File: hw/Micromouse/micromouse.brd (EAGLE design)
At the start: 60 x 112 mm, 44 parts, among them IC1 DSPIC33FJ64MC804-PT, IC2 DRV8833PWR, J1 GP2Y0A51SK0F, J2 GP2Y0A51SK0F, J3 GP2Y0A41SK0F, SW1 B3F-1000

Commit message: Updated PCB
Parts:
- added C15, C16, C17: (no value), micromouse:0805_POL
- moved C12 29.2 mm to (-5.00, -38.2), turned to 270 degrees
- moved SW1 27.6 mm to (-0.04, -36.9)
- moved R4 26.9 mm to (-7.20, -36.0)
- moved R5 21.4 mm to (-5.00, -33.8), turned to 90 degrees
- moved R3 11.8 mm to (-19.6, 40.9), turned to 90 degrees
- moved SW_RST 10.3 mm to (-25.4, 38.6), turned to 0 degrees
- moved R2 10.0 mm to (-25.4, 44.7), turned to 331.7 degrees
- moved LED1 9.80 mm to (0.00, 51.2)
- moved D4 9.47 mm to (-24.4, 47.7), turned to 151.7 degrees
- moved D3 9.46 mm to (-23.4, 49.6), turned to 151.7 degrees
- moved D2 9.45 mm to (-22.4, 51.4), turned to 151.7 degrees
- moved D1 9.44 mm to (-21.5, 53.2), turned to 151.7 degrees
- moved R9 9.42 mm to (-21.0, 45.6), turned to 331.7 degrees
- moved R8 9.41 mm to (-20.0, 47.6), turned to 331.7 degrees
- moved R7 9.41 mm to (-19.0, 49.6), turned to 331.7 degrees
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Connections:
- net +5V: now also C15.1, C16.1, C17.1
- net GND: now also C15.2, C16.2, C17.2
- net S1_OUT: now also IC1.22; no longer IC1.20
- net S3_OUT: now also IC1.20; no longer IC1.22
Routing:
- net +3V3: track 267.4 -> 279.6 mm, vias 5 -> 4
- net SW1: track 54.9 -> 66.8 mm, vias 4 -> 2
- net +5V: track 118.8 -> 125.7 mm
- net GND: track 52.7 -> 58.3 mm, vias 19 -> 20
- net S1_OUT: track 21.6 -> 27.3 mm
- net S2_OUT: track 19.1 -> 22.3 mm
- net N$7: track 10.8 -> 13.6 mm
- net LED4: track 15.7 -> 17.6 mm
- net N$6: track 7.98 -> 9.81 mm
- net LED3: track 16.3 -> 18.0 mm
- net S3_OUT: track 10.2 -> 8.64 mm
- net +9V: track 88.2 -> 87.0 mm
- net LED2: track 17.0 -> 18.0 mm
- net MCLR: track 31.7 -> 31.0 mm
- net M2-: track 16.3 -> 16.9 mm
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- added copper zone on layer 1, net GND
- added copper zone on layer 16, net GND
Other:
- board size 60 x 112 mm -> 60 x 97 mm

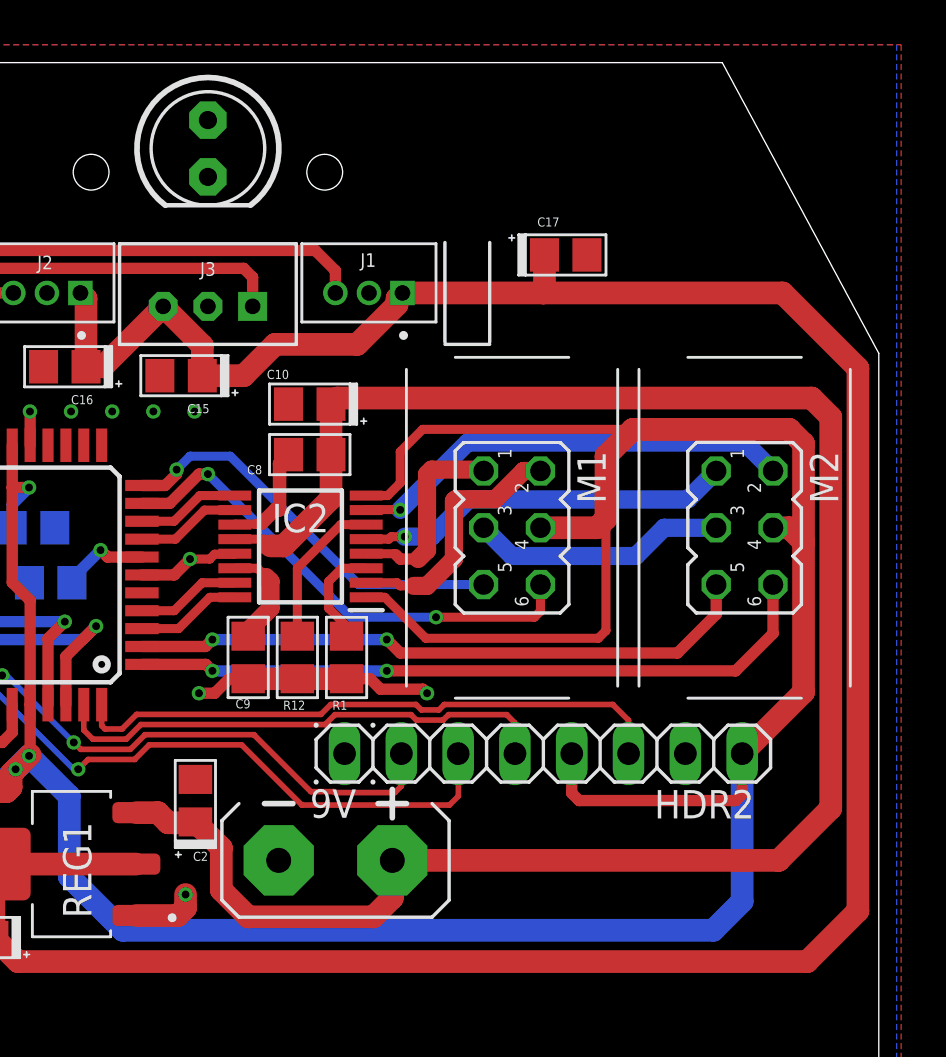
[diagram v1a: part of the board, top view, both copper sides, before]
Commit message: Added hole for routing wires of battery connector
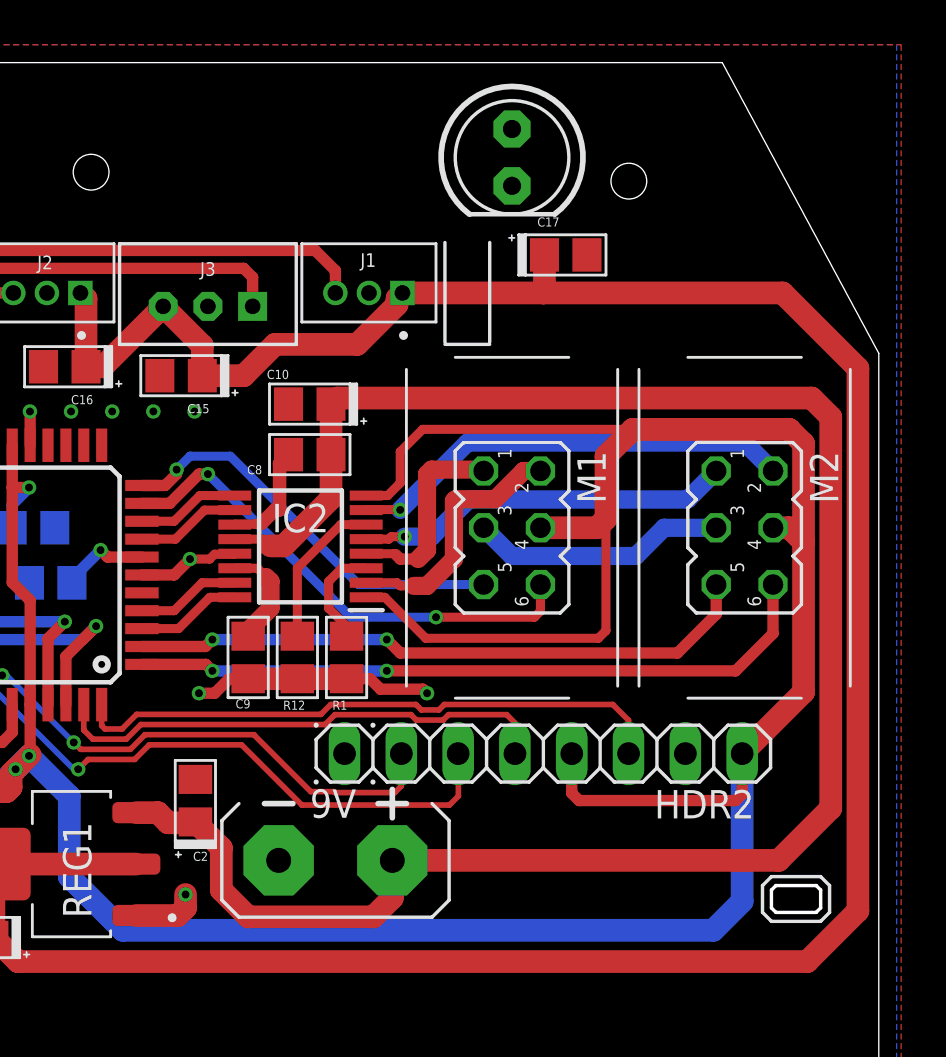
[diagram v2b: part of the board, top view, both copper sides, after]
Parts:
- moved LED1 13.6 mm to (13.6, 50.8)
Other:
- outline, holes or cut-outs redrawn
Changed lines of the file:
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@@
 <drawing>
 <settings>
-<setting alwaysvectorfont="no"/>
+<setting alwaysvectorfont="yes"/>
 <setting verticaltext="up"/>
 </settings>
@@
 </layers>
 <board>
-<fusionsync huburn="a.YnVzaW5lc3M6bXl0dW05MzU" projecturn="a.YnVzaW5lc3M6bXl0dW05MzUjMjAyMTAxMTgzNzI4NzA0MjY" f3durn="urn:adsk.wipprod:dm.lineage:L23jFv8gR_u2aycr5DJv9Q" pcbguid="" lastpulledtime="2021-02-11T09:58:18Z" lastsyncedchangeguid="" latestrevisionid="4fbf5507-91a6-4be1-affa-b37500ad01a3" lastsyncedrevisionid="4fbf5507-91a6-4be1-affa-b37500ad01a3" lastboardhashguid="931b2172-0a8d-4494-72eb-2a34aca0cbeb" lastpushedtime="2021-02-11T20:43:38Z" linktopcb3d="true"/>
+<fusionsync huburn="a.YnVzaW5lc3M6bXl0dW05MzU" projecturn="a.YnVzaW5lc3M6bXl0dW05MzUjMjAyMTAxMTgzNzI4NzA0MjY" f3durn="urn:adsk.wipprod:dm.lineage:L23jFv8gR_u2aycr5DJv9Q" pcbguid="" lastpulledtime="2021-02-11T09:58:18Z" lastsyncedchangeguid="" latestrevisionid="bb3ab1a6-1e4b-46e2-9ee9-392ab2f42304" lastsyncedrevisionid="bb3ab1a6-1e4b-46e2-9ee9-392ab2f42304" lastboardhashguid="8f49f6ad-d1e3-cec0-48bd-d1e4115f87a2" lastpushedtime="2021-02-16T11:45:34Z" linktopcb3d="true"/>
 <plain>
 <wire x1="10.598" y1="46.956" x2="10.598" y2="42.498" width="0.1524" layer="21"/>
@@
 <wire x1="12.6" y1="42.4" x2="10.6" y2="42.4" width="0.1524" layer="21"/>
 <wire x1="12.602" y1="46.956" x2="12.602" y2="42.498" width="0.1524" layer="21"/>
-<circle x="5.223" y="50.1" radius="0.8" width="0" layer="20"/>
+<circle x="18.823" y="49.7" radius="0.8" width="0" layer="20"/>
 <circle x="21" y="2" radius="0.8" width="0" layer="20"/>
 <circle x="21" y="-40" radius="0.8" width="0" layer="20"/>
@@
 <wire x1="23" y1="55" x2="-23" y2="55" width="0" layer="20"/>
 <wire x1="-23" y1="55" x2="-30" y2="42" width="0" layer="20"/>
+<wire x1="27.4" y1="18" x2="27.2" y2="18.2" width="0.1524" layer="20"/>
+<wire x1="27.2" y1="18.2" x2="25.4" y2="18.2" width="0.1524" layer="20"/>
+<wire x1="25.4" y1="18.2" x2="25.2" y2="18" width="0.1524" layer="20"/>
+<wire x1="25.2" y1="17.2" x2="25.4" y2="17" width="0.1524" layer="20"/>
+<wire x1="25.4" y1="17" x2="27.2" y2="17" width="0.1524" layer="20"/>
+<wire x1="27.2" y1="17" x2="27.4" y2="17.2" width="0.1524" layer="20"/>
+<wire x1="27.4" y1="18" x2="27.4" y2="17.2" width="0.1524" layer="20"/>
+<wire x1="25.2" y1="17.2" x2="25.2" y2="18" width="0.1524" layer="20"/>
+<wire x1="25.2" y1="18.6" x2="27.4" y2="18.6" width="0.1524" layer="21"/>
+<wire x1="27.4" y1="18.6" x2="27.8" y2="18.2" width="0.1524" layer="21"/>
+<wire x1="27.8" y1="18.2" x2="27.8" y2="17" width="0.1524" layer="21"/>
+<wire x1="27.8" y1="17" x2="27.4" y2="16.6" width="0.1524" layer="21"/>
+<wire x1="27.4" y1="16.6" x2="25.2" y2="16.6" width="0.1524" layer="21"/>
+<wire x1="25.2" y1="16.6" x2="24.8" y2="17" width="0.1524" layer="21"/>
+<wire x1="24.8" y1="17" x2="24.8" y2="18.2" width="0.1524" layer="21"/>
+<wire x1="24.8" y1="18.2" x2="25.2" y2="18.6" width="0.1524" layer="21"/>
 </plain>
 <attributes>
@@
 <attribute name="VALUE" x="4.14" y="30.825" size="1.27" layer="27" rot="R180" align="center"/>
 </element>
-<element name="LED1" library="adafruit" library_urn="urn:adsk.eagle:library:420" package="LED5MM" package3d_urn="urn:adsk.eagle:package:6240538/1" value="" x="0" y="51.16" smashed="yes" rot="R270">
-<attribute name="VALUE" x="-1.8034" y="47.9596" size="1.27" layer="27" ratio="10" rot="R270"/>
+<element name="LED1" library="adafruit" library_urn="urn:adsk.eagle:library:420" package="LED5MM" package3d_urn="urn:adsk.eagle:package:6240538/1" value="" x="13.6" y="50.76" smashed="yes" rot="R270">
+<attribute name="VALUE" x="11.7966" y="47.5596" size="1.27" layer="27" ratio="10" rot="R270"/>
 </element>
 <element name="C1" library="micromouse" library_urn="urn:adsk.eagle:library:26475156" package="0805_POL" package3d_urn="urn:adsk.eagle:package:26475189/5" value="10u" x="-7.03" y="31.74" smashed="yes" rot="MR0">

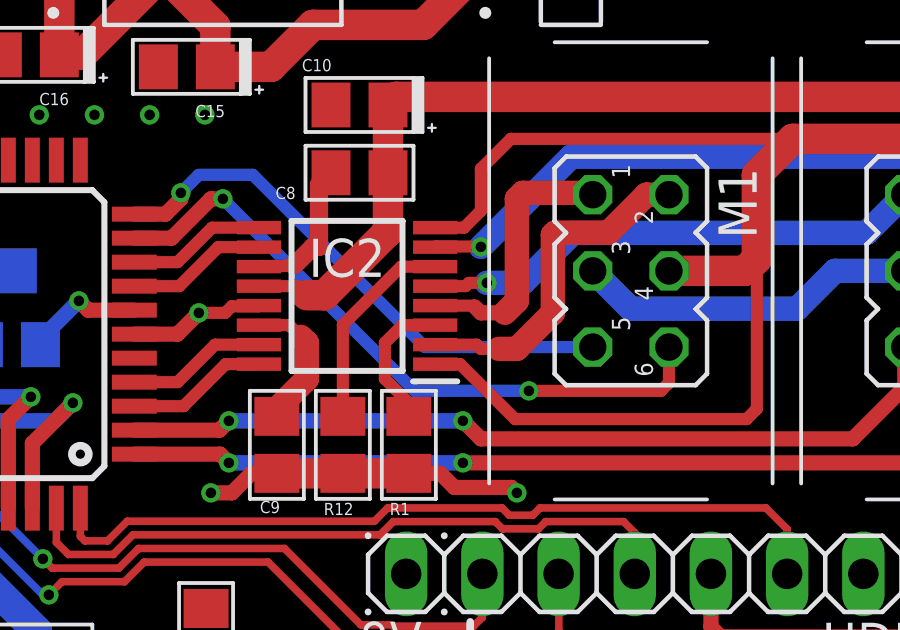
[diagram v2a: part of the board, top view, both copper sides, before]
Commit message: Tidied up schematic
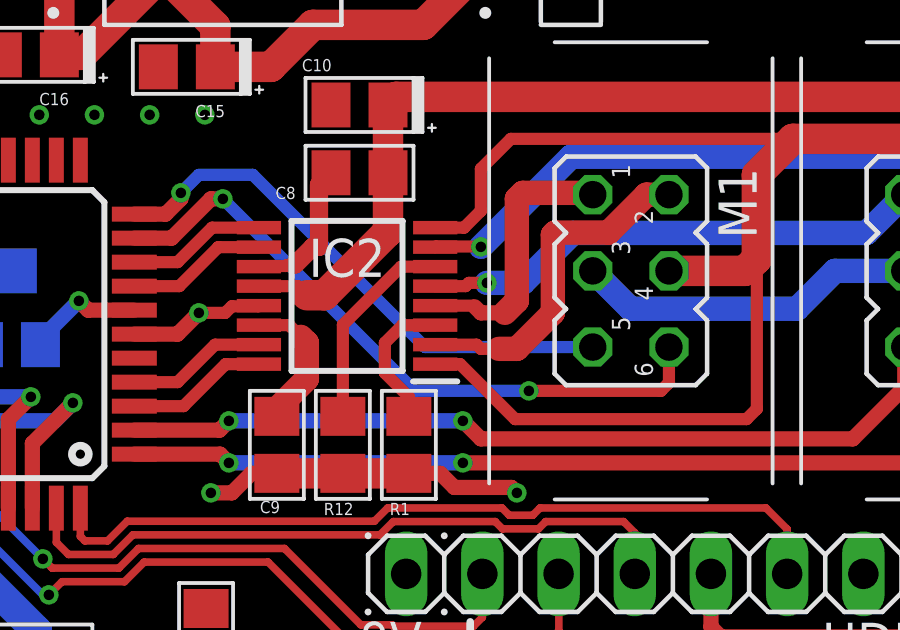
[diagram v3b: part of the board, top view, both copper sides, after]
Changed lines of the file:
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@@
 <drawing>
 <settings>
-<setting alwaysvectorfont="yes"/>
+<setting alwaysvectorfont="no"/>
 <setting verticaltext="up"/>
 </settings>
@@
 <contactref element="R1" pad="2"/>
 <contactref element="C10" pad="2"/>
-<contactref element="SW_RST" pad="2"/>
 <contactref element="SW1" pad="2"/>
 <contactref element="C12" pad="2"/>
 <contactref element="HDR1" pad="3"/>
-<contactref element="J3" pad="2"/>
-<contactref element="J1" pad="2"/>
-<contactref element="J2" pad="2"/>
 <contactref element="R12" pad="2"/>
 <contactref element="C14" pad="1"/>
@@
 <wire x1="-23.193" y1="21.2" x2="-24.8" y2="21.2" width="1.016" layer="1"/>
 <via x="-24.8" y="21.2" extent="1-16" drill="0.35"/>
-<contactref element="C15" pad="2"/>
-<contactref element="C16" pad="2"/>
-<contactref element="C17" pad="2"/>
 <wire x1="-24" y1="28.2" x2="-24" y2="32.6" width="0.6096" layer="1"/>
 <wire x1="-24" y1="32.6" x2="-24.2" y2="32.8" width="0.6096" layer="1"/>
@@
 <vertex x="-30.4" y="54"/>
 </polygon>
+<contactref element="SW_RST" pad="2"/>
+<contactref element="J3" pad="2"/>
+<contactref element="J1" pad="2"/>
+<contactref element="J2" pad="2"/>
+<contactref element="C15" pad="2"/>
+<contactref element="C16" pad="2"/>
+<contactref element="C17" pad="2"/>
 </signal>
 <signal name="+3V3">
@@
 <contactref element="M1" pad="4"/>
 <contactref element="M2" pad="4"/>
-<contactref element="IC2" pad="8"/>
-<contactref element="IC2" pad="1"/>
 <contactref element="R2" pad="1"/>
 <contactref element="R4" pad="1"/>
@@
 <wire x1="17.4" y1="34.2" x2="14.87" y2="34.2" width="1.016" layer="1"/>
 <wire x1="17.8" y1="37.4" x2="17.8" y2="34.6" width="1.016" layer="1"/>
-<wire x1="7.078" y1="35.64" x2="8.04" y2="35.64" width="0.4064" layer="1"/>
-<wire x1="7.078" y1="31.09" x2="7.91" y2="31.09" width="0.4064" layer="1"/>
 <wire x1="17.4572" y1="29.2572" x2="17.8" y2="29.6" width="0.4064" layer="1"/>
 <wire x1="17.8" y1="29.6" x2="17.8" y2="34.6" width="0.4064" layer="1"/>
-<wire x1="7.91" y1="31.09" x2="9.7428" y2="29.2572" width="0.4064" layer="1"/>
+<wire x1="9.7428" y1="29.2572" x2="7.91" y2="31.09" width="0.4064" layer="1"/>
 <wire x1="9.7428" y1="29.2572" x2="17.4572" y2="29.2572" width="0.4064" layer="1"/>
 <wire x1="-7.95" y1="26.29" x2="-7.95" y2="30.95" width="0.508" layer="1"/>
@@
 <wire x1="-10.95" y1="-35.05" x2="-7.2" y2="-35.05" width="0.8128" layer="1"/>
 <wire x1="-15" y1="-31" x2="-10.95" y2="-35.05" width="0.8128" layer="1"/>
-<wire x1="8.04" y1="35.64" x2="8.6" y2="36.2" width="0.4064" layer="1"/>
+<wire x1="8.6" y1="36.2" x2="8.04" y2="35.64" width="0.4064" layer="1"/>
 <wire x1="9.6" y1="38.6" x2="19" y2="38.6" width="0.4064" layer="1"/>
 <wire x1="8.6" y1="36.2" x2="8.6" y2="37.6" width="0.4064" layer="1"/>
@@
 <wire x1="-26.8" y1="43.4" x2="-24.708" y2="41.308" width="0.508" layer="1"/>
 <wire x1="-24.708" y1="41.308" x2="-24.708" y2="37.708" width="0.508" layer="1"/>
+<contactref element="IC2" pad="8"/>
+<contactref element="IC2" pad="1"/>
+<wire x1="8.04" y1="35.64" x2="7.078" y2="35.64" width="0.4064" layer="1"/>
+<wire x1="7.91" y1="31.09" x2="7.078" y2="31.09" width="0.4064" layer="1"/>
 </signal>
 <signal name="VCAP/VDDCORE">
@@
 </signal>
 <signal name="N$5">
-<contactref element="R1" pad="1"/>
 <contactref element="IC2" pad="3"/>
 <wire x1="7.078" y1="32.39" x2="5.99" y2="32.39" width="0.4064" layer="1"/>
-<wire x1="5.4" y1="31.8" x2="5.4" y2="30.6" width="0.4064" layer="1"/>
-<wire x1="6.2" y1="29.8" x2="6.2" y2="29.35" width="0.4064" layer="1"/>
+<wire x1="5.4" y1="31.8" x2="5.4" y2="30.8" width="0.4064" layer="1"/>
 <wire x1="5.99" y1="32.39" x2="5.4" y2="31.8" width="0.4064" layer="1"/>
-<wire x1="5.4" y1="30.6" x2="6.2" y2="29.8" width="0.4064" layer="1"/>
+<contactref element="R1" pad="1"/>
+<wire x1="6.2" y1="30" x2="6.2" y2="29.35" width="0.4064" layer="1"/>
+<wire x1="5.4" y1="30.8" x2="6.2" y2="30" width="0.4064" layer="1"/>
 </signal>
 <signal name="M1_IN1">
@@
 <wire x1="-10.1" y1="44.7" x2="-8.7" y2="44.7" width="0.508" layer="1"/>
 <wire x1="-11.15" y1="43.65" x2="-10.1" y2="44.7" width="0.508" layer="1"/>
-</signal>
-<signal name="N$1">
-<contactref element="IC2" pad="6"/>
-<contactref element="R12" pad="1"/>
-<wire x1="7.078" y1="34.34" x2="5.94" y2="34.34" width="0.4064" layer="1"/>
-<wire x1="4" y1="32.4" x2="4" y2="29.35" width="0.4064" layer="1"/>
-<wire x1="5.94" y1="34.34" x2="4" y2="32.4" width="0.4064" layer="1"/>
 </signal>
 <signal name="BT_RTS">
@@
 <wire x1="-20.669959375" y1="50.05790625" x2="-19.860975" y2="50.064890625" width="0.508" layer="1"/>
 </signal>
+<signal name="N$1">
+<contactref element="IC2" pad="6"/>
+<wire x1="7.078" y1="34.34" x2="5.94" y2="34.34" width="0.4064" layer="1"/>
+<wire x1="5.94" y1="34.34" x2="4" y2="32.4" width="0.4064" layer="1"/>
+<contactref element="R12" pad="1"/>
+<wire x1="4" y1="32.4" x2="4" y2="29.35" width="0.4064" layer="1"/>
+</signal>
 </signals>

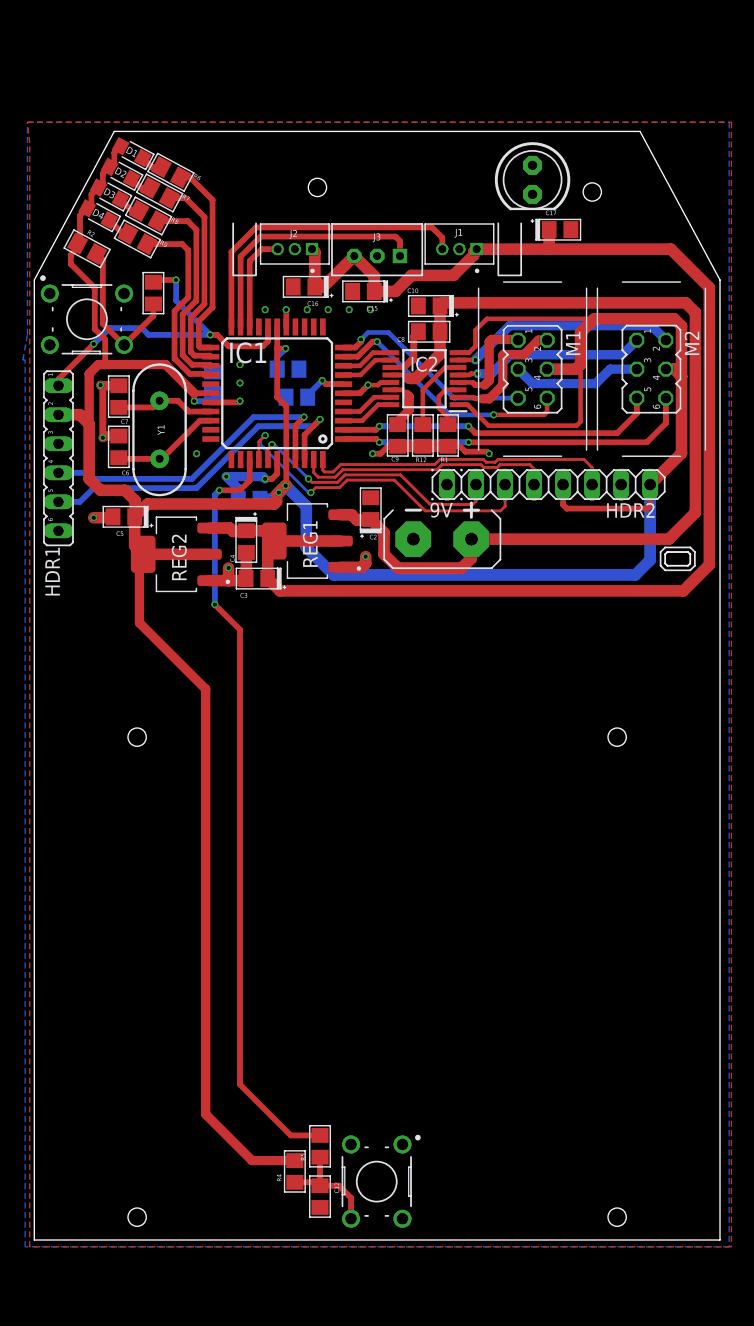
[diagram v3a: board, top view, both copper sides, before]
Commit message: Updated silkscreen
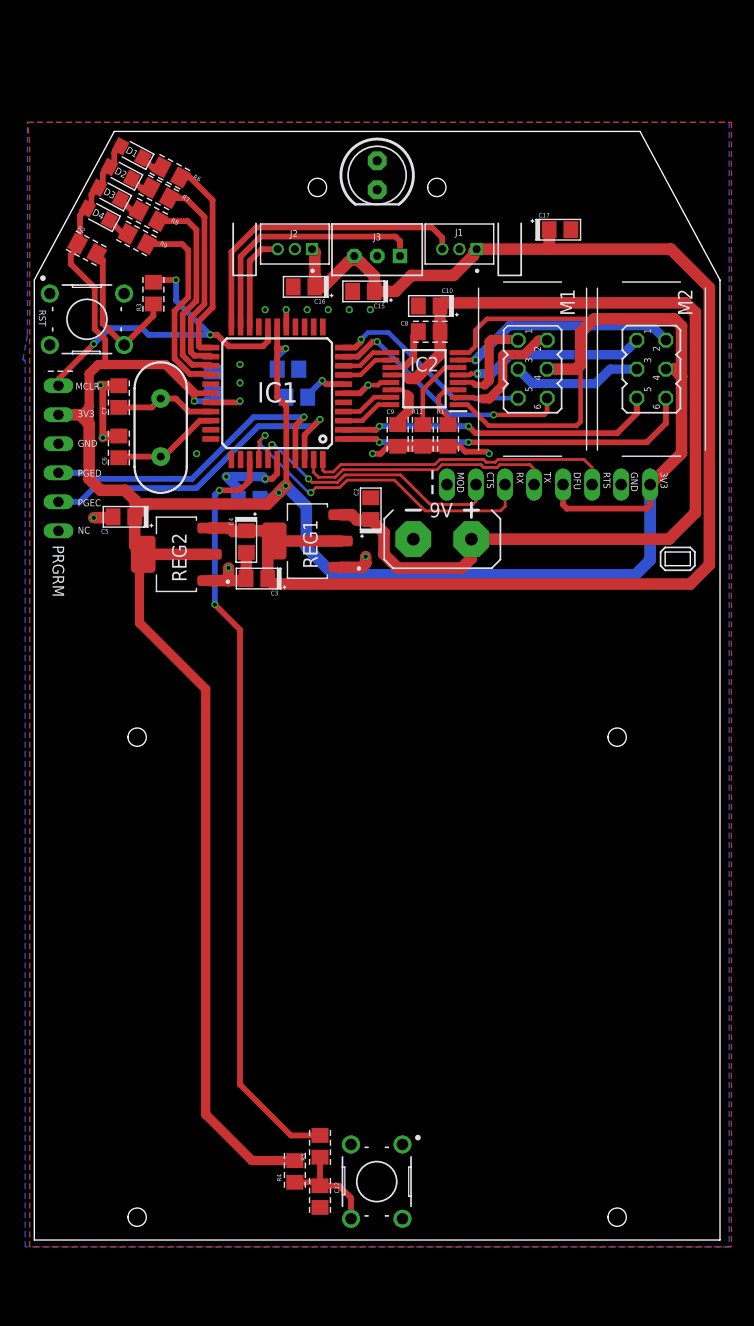
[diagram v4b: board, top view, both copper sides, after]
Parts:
- moved LED1 13.6 mm to (0.00, 51.2)
- moved Y1 0.22 mm to (-18.9, 29.1)
- turned D2 to 152 degrees
- turned D3 to 152 degrees
- turned R8 to 332 degrees
- turned D4 to 152 degrees
- turned D1 to 152 degrees
- turned R9 to 332 degrees
- turned R7 to 332 degrees
- turned R2 to 332 degrees
- turned R6 to 332 degrees
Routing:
- net +3V3: track 279.6 -> 281.6 mm
- net +5V: track 125.7 -> 127.7 mm
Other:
- outline, holes or cut-outs redrawn
- board text added: "3V3"
- board text added: "CTS"
- board text added: "DFU"
- board text added: "GND"
- board text added: "MCLR"
- board text added: "MOD"
- board text added: "NC"
- board text added: "PGEC"
- board text added: "PGED"
- board text added: "PRGRM"
- board text added: "RST"
- board text added: "RTS"
- board text added: "RX"
- board text added: "TX"
